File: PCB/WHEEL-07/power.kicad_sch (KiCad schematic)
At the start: 21 parts, among them IC1 LDO40LPU33RY, IC2 LDO40LPU50RY, Q1 AO3401A

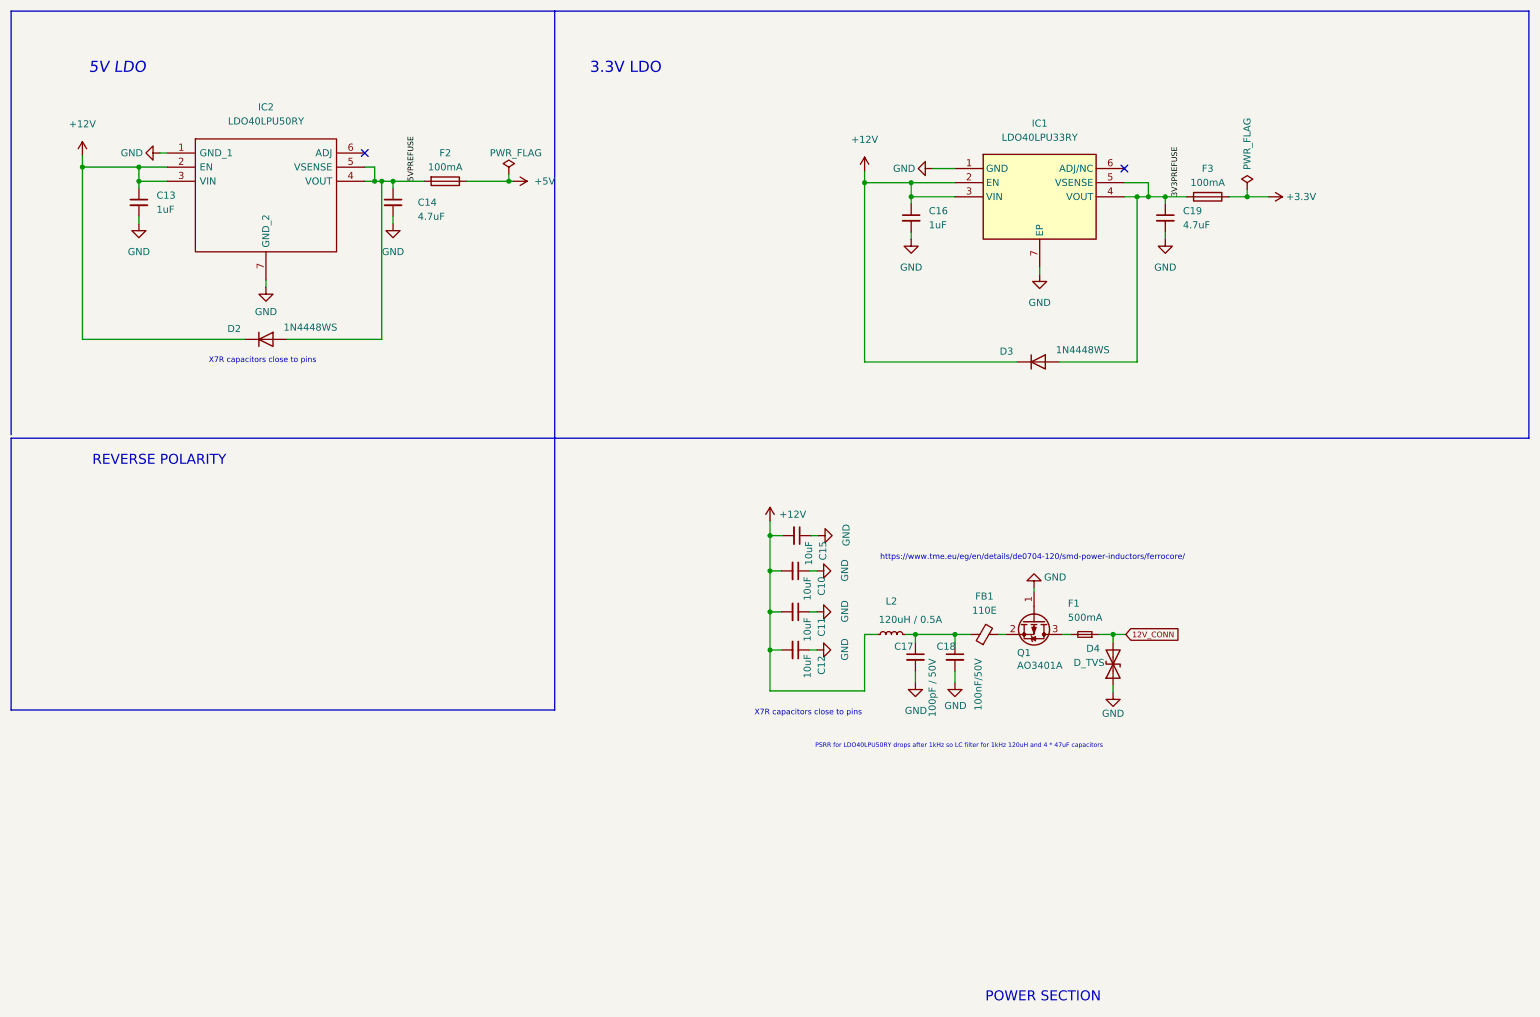
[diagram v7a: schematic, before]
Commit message: Revised board with 2 x LDO40 and cleaned-up schematics
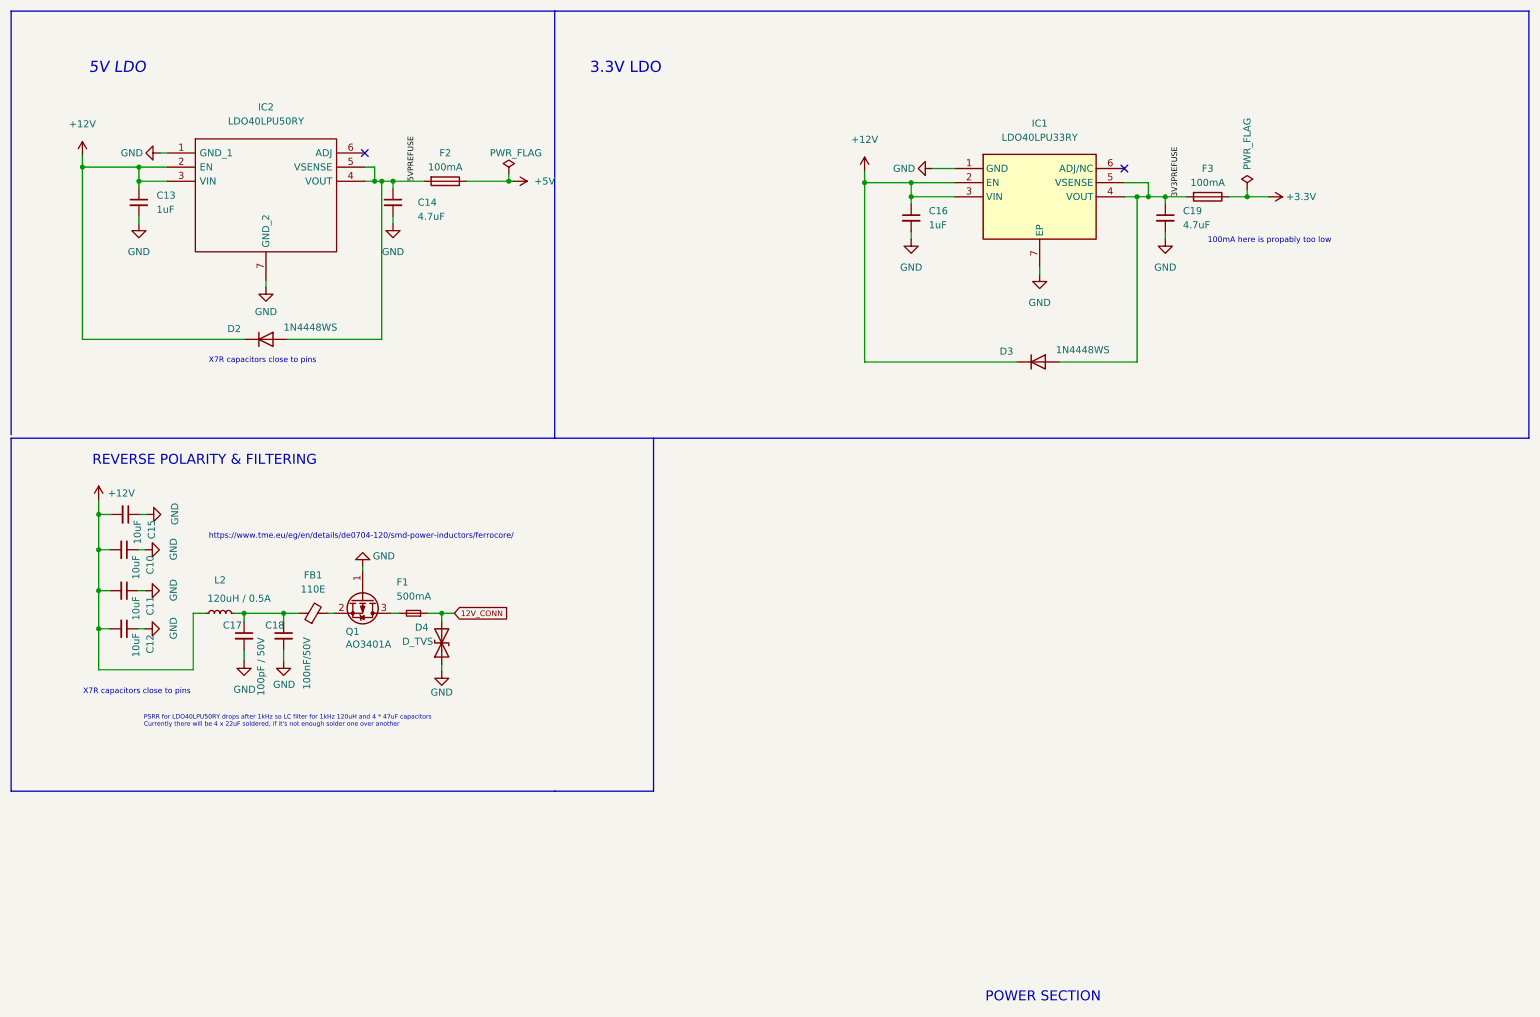
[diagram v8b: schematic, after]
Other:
- note added: "100mA here is propably too low"
- note added: "PSRR for LDO40LPU50RY drops after 1kHz so LC filter for 1kHz 120uH and 4 * 47uF capacitors Currently there will be 4 x 22uF soldered, if it's not enough solder one over another"
- note added: "REVERSE POLARITY & FILTERING"
- note removed: "PSRR for LDO40LPU50RY drops after 1kHz so LC filter for 1kHz 120uH and 4 * 47uF capacitors"
- note removed: "REVERSE POLARITY"
- moved on the sheet: C10, C11, C12, C15, C17, C18, D4, F1, FB1, L2, Q1
